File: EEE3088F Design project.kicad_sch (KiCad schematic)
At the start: 0 parts

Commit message: changes made
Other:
- added sheet motor connections (main.kicad_sch)
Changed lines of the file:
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@@
 		(comment 4 "Phila Haanyama, Hannah Owen")
+	)
+	(sheet
+		(at 53.34 41.91)
+		(size 34.29 24.13)
+		(exclude_from_sim no)
+		(in_bom yes)
+		(on_board yes)
+		(dnp no)
+		(fields_autoplaced yes)
+		(stroke
+			(width 0.1524)
+			(type solid)
+		)
+		(fill
+			(color 0 0 0 0.0000)
+		)
+		(property "Sheetname" "motor connections"
+			(at 53.34 41.1984 0)
+			(show_name yes)
+			(effects
+				(font
+					(size 1.27 1.27)
+				)
+				(justify left bottom)
+			)
+		)
+		(property "Sheetfile" "main.kicad_sch"
+			(at 53.34 66.6246 0)
+			(effects
+				(font
+					(size 1.27 1.27)
+				)
+				(justify left top)
+			)
+		)
+		(instances
+			(project "EEE3088F Design project"
+				(path "/d1463c6f-2f5e-4460-8cd2-c7ccf4d8def7"
+					(page "2")
+				)
+			)
+		)
 	)
 	(sheet_instances

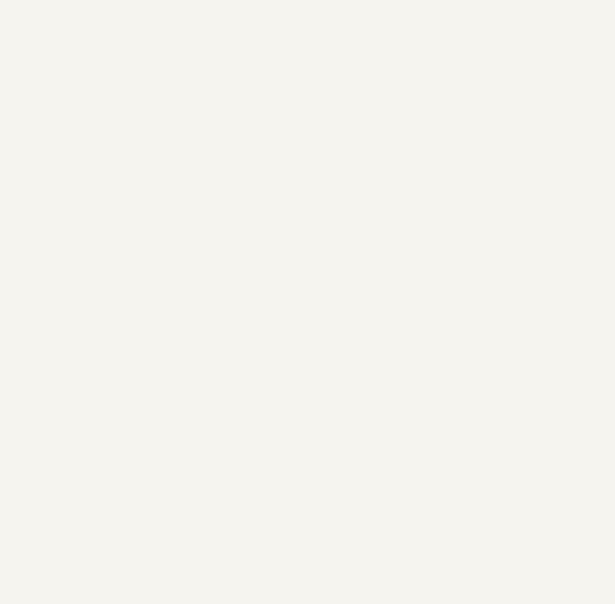
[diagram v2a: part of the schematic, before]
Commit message: Updated KiCad project files and removed old backups
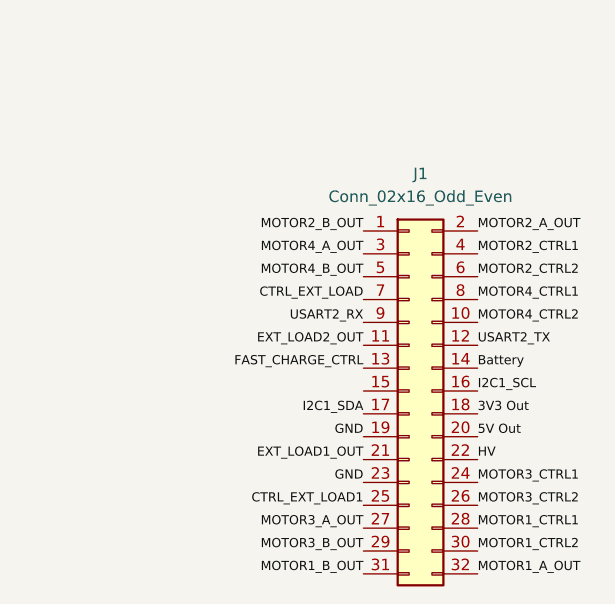
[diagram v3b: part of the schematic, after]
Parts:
- added J1: Conn_02x16_Odd_Even, symbol Connector_Generic:Conn_02x16_Odd_Even
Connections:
- new net 3V3 Out: J1.18 (Pin_18)
- new net 5V Out: J1.20 (Pin_20)
- new net Battery: J1.14 (Pin_14)
- new net CTRL_EXT_LOAD: J1.7 (Pin_7)
- new net CTRL_EXT_LOAD1: J1.25 (Pin_25)
- new net EXT_LOAD1_OUT: J1.21 (Pin_21)
- new net EXT_LOAD2_OUT: J1.11 (Pin_11)
- new net FAST_CHARGE_CTRL: J1.13 (Pin_13)
- new net GND: J1.19 (Pin_19), J1.23 (Pin_23)
- new net HV: J1.22 (Pin_22)
- new net I2C1_SCL: J1.16 (Pin_16)
- new net I2C1_SDA: J1.17 (Pin_17)
- new net MOTOR1_A_OUT: J1.32 (Pin_32)
- new net MOTOR1_B_OUT: J1.31 (Pin_31)
- new net MOTOR1_CTRL1: J1.28 (Pin_28)
- new net MOTOR1_CTRL2: J1.30 (Pin_30)
- new net MOTOR2_A_OUT: J1.2 (Pin_2)
- new net MOTOR2_B_OUT: J1.1 (Pin_1)
- new net MOTOR2_CTRL1: J1.4 (Pin_4)
- new net MOTOR2_CTRL2: J1.6 (Pin_6)
- new net MOTOR3_A_OUT: J1.27 (Pin_27)
- new net MOTOR3_B_OUT: J1.29 (Pin_29)
- new net MOTOR3_CTRL1: J1.24 (Pin_24)
- new net MOTOR3_CTRL2: J1.26 (Pin_26)
- new net MOTOR4_A_OUT: J1.3 (Pin_3)
- new net MOTOR4_B_OUT: J1.5 (Pin_5)
- new net MOTOR4_CTRL1: J1.8 (Pin_8)
- new net MOTOR4_CTRL2: J1.10 (Pin_10)
- new net USART2_RX: J1.9 (Pin_9)
- new net USART2_TX: J1.12 (Pin_12)

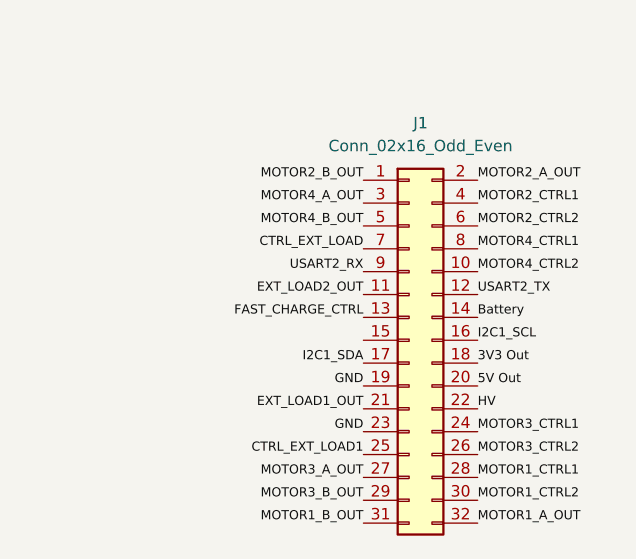
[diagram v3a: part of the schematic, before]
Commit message: DNP for 2x16 and global labels
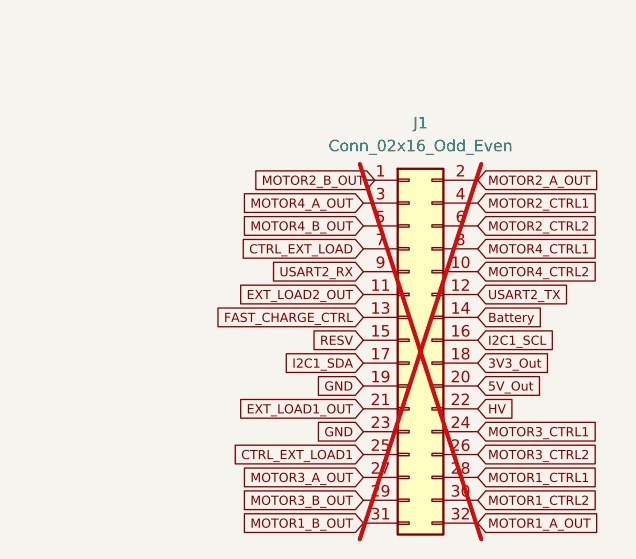
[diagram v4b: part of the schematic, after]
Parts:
- J1: now not fitted
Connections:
- net RESV: now reaches J1.15 (Pin_15)
- net 3V3 Out renamed 3V3_Out
- net 5V Out renamed 5V_Out

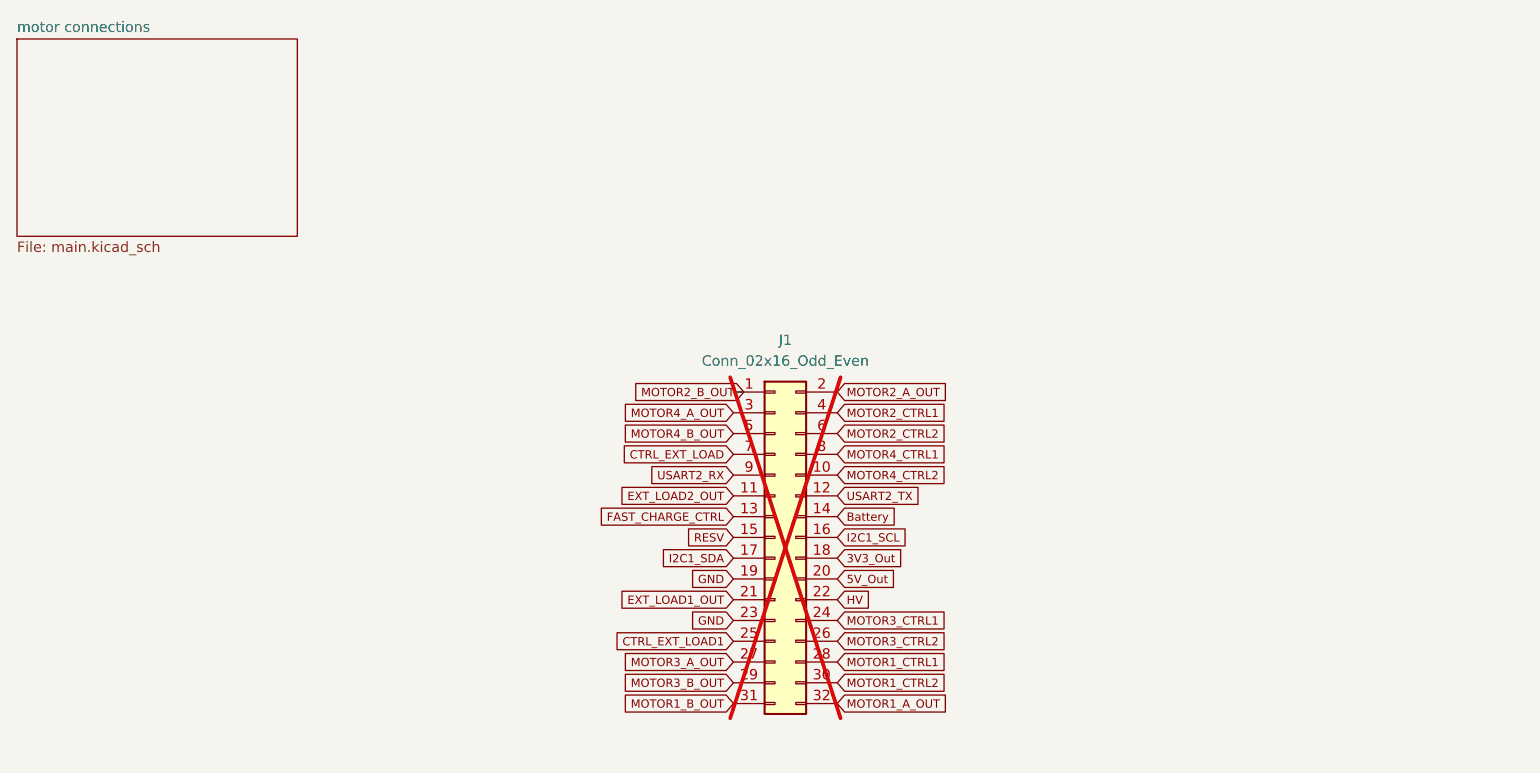
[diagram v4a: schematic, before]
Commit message: Removed old backups and updated KiCad files
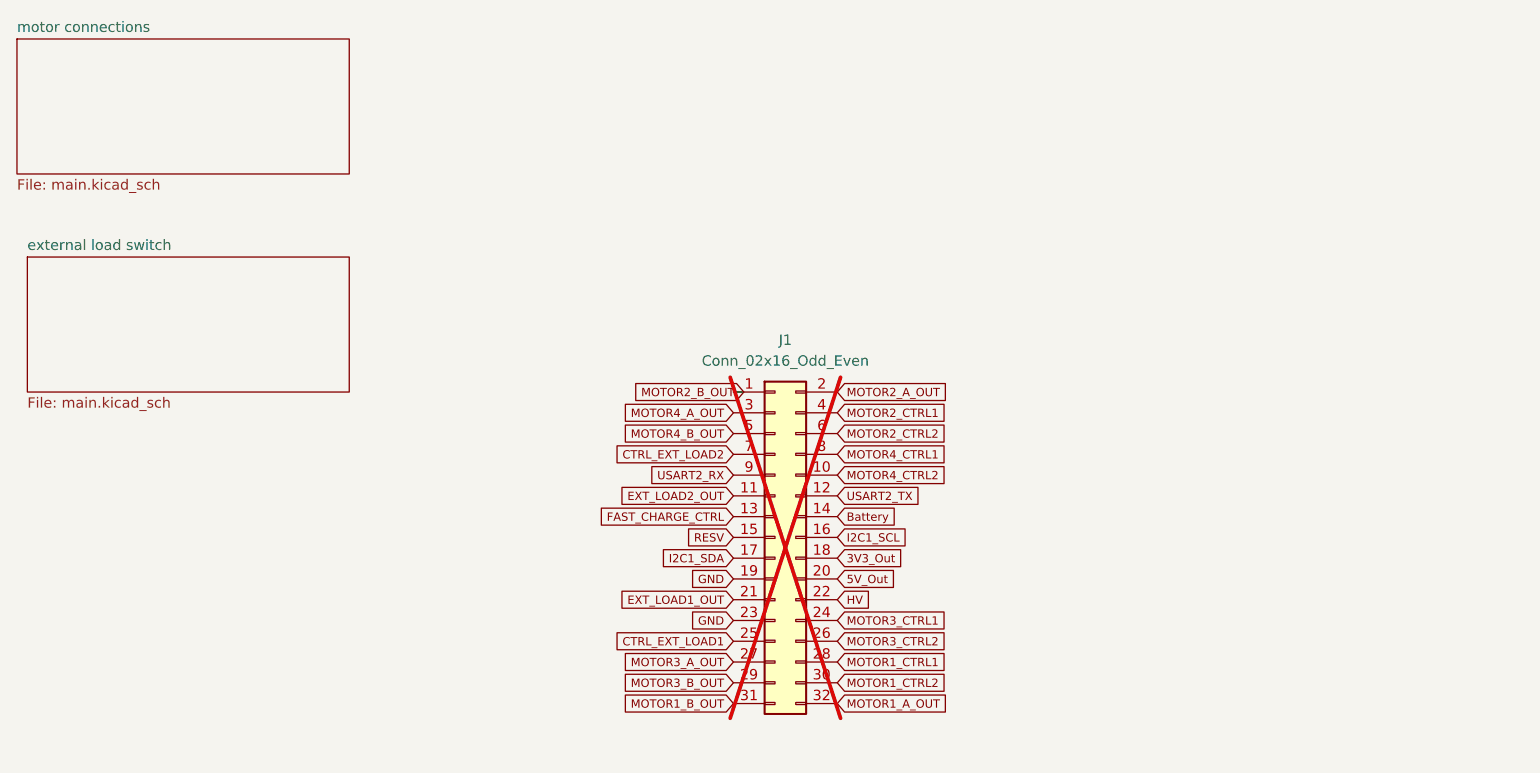
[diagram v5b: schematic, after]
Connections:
- net CTRL_EXT_LOAD renamed CTRL_EXT_LOAD2
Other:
- added sheet external load switch (main.kicad_sch)
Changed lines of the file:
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@@
 		)
 	)
-	(global_label "CTRL_EXT_LOAD"
+	(global_label "CTRL_EXT_LOAD2"
 		(shape input)
 		(at 140.97 92.71 180)
@@
 		)
 		(property "Intersheetrefs" "${INTERSHEET_REFS}"
-			(at 126.9706 92.71 0)
+			(at 126.003 92.71 0)
 			(effects
 				(font
@@
 	(sheet
 		(at 53.34 41.91)
-		(size 34.29 24.13)
+		(size 40.64 16.51)
 		(exclude_from_sim no)
 		(in_bom yes)
@@
 		)
 		(property "Sheetfile" "main.kicad_sch"
-			(at 53.34 66.6246 0)
+			(at 53.34 59.0046 0)
 			(effects
 				(font
@@
 				)
 			)
+		)
+	)
+	(sheet
+		(at 54.61 68.58)
+		(size 39.37 16.51)
+		(exclude_from_sim no)
+		(in_bom yes)
+		(on_board yes)
+		(dnp no)
+		(fields_autoplaced yes)
+		(stroke
+			(width 0.1524)
+			(type solid)
+		)
+		(fill
+			(color 0 0 0 0.0000)
+		)
+		(property "Sheetname" "external load switch"
+			(at 54.61 67.8684 0)
+			(show_name yes)
+			(effects
+				(font
+					(size 1.27 1.27)
+				)
+				(justify left bottom)
+			)
+		)
+		(property "Sheetfile" "main.kicad_sch"
+			(at 54.61 85.6746 0)
+			(effects
+				(font
+					(size 1.27 1.27)
+				)
+				(justify left top)
+			)
+		)
+		(instances
+			(project "EEE3088F Design project"
+				(path "/d1463c6f-2f5e-4460-8cd2-c7ccf4d8def7"
+					(page "3")
+				)
+			)

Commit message: added motor and INA219 circuits
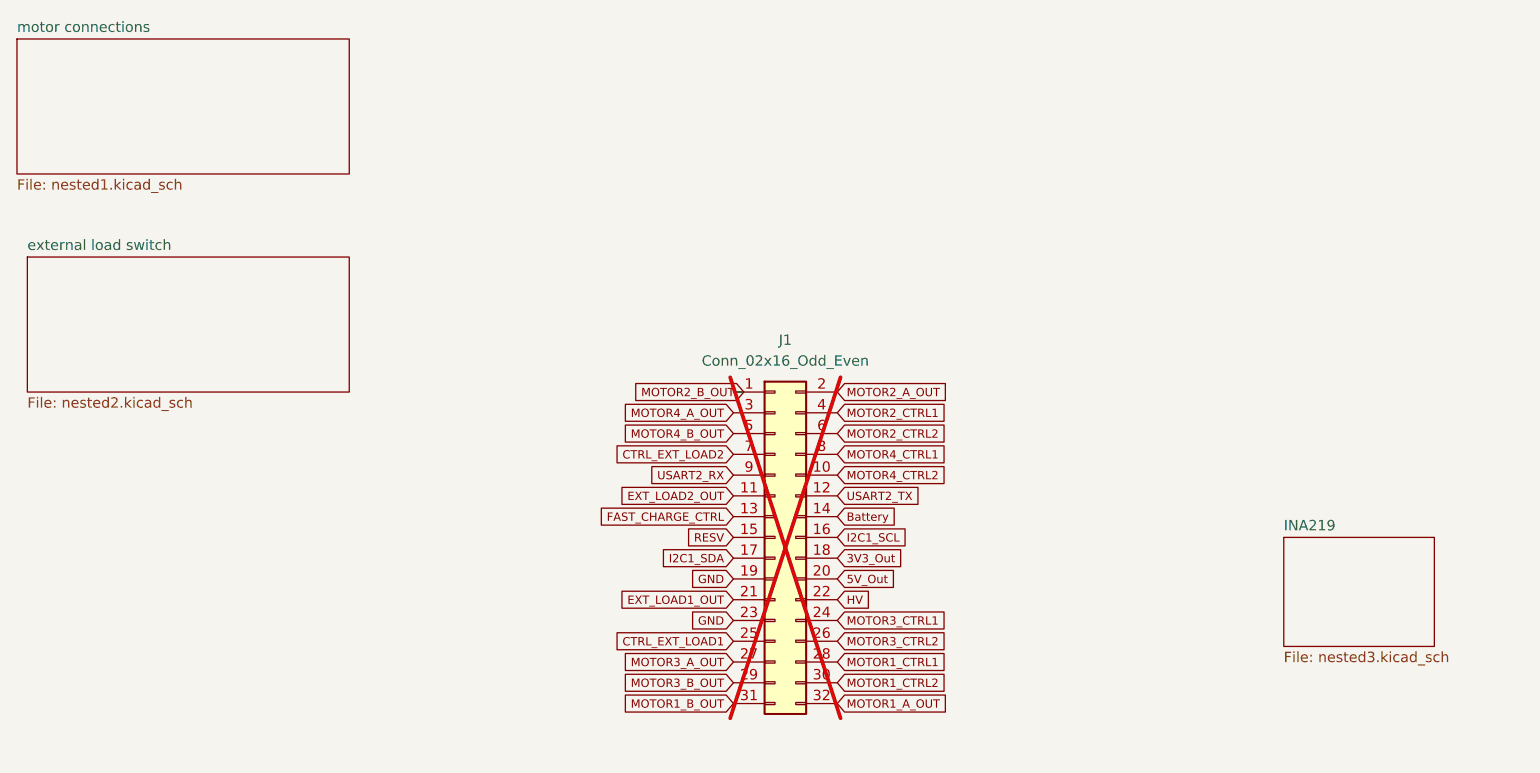
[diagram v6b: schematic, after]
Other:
- added sheet INA219 (nested3.kicad_sch)
- sheet external load switch: file main.kicad_sch -> nested2.kicad_sch
- sheet motor connections: file main.kicad_sch -> nested1.kicad_sch
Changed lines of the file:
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@@
 			)
 		)
-		(property "Sheetfile" "main.kicad_sch"
+		(property "Sheetfile" "nested1.kicad_sch"
 			(at 53.34 59.0046 0)
 			(effects
@@
 			)
 		)
-		(property "Sheetfile" "main.kicad_sch"
+		(property "Sheetfile" "nested2.kicad_sch"
 			(at 54.61 85.6746 0)
 			(effects
 				(font
+					(size 1.27 1.27)
+				)
+				(justify left top)
+			)
+		)
+		(instances
+			(project "EEE3088F Design project"
+				(path "/d1463c6f-2f5e-4460-8cd2-c7ccf4d8def7"
+					(page "3")
+				)
+			)
+		)
+	)
+	(sheet
+		(at 208.28 102.87)
+		(size 18.415 13.335)
+		(exclude_from_sim no)
+		(in_bom yes)
+		(on_board yes)
+		(dnp no)
+		(fields_autoplaced yes)
+		(stroke
+			(width 0.1524)
+			(type solid)
+		)
+		(fill
+			(color 0 0 0 0.0000)
+		)
+		(property "Sheetname" "INA219"
+			(at 208.28 102.1584 0)
+			(effects
+				(font
+					(size 1.27 1.27)
+				)
+				(justify left bottom)
+			)
+		)
+		(property "Sheetfile" "nested3.kicad_sch"
+			(at 208.28 116.7896 0)
+			(effects
+				(font

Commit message: made changes to USB circuit
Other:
- added sheet USB C (nested4.kicad_sch)
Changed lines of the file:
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@@
+		)
+	)
+	(sheet
+		(at 210.058 74.676)
+		(size 18.542 12.954)
+		(exclude_from_sim no)
+		(in_bom yes)
+		(on_board yes)
+		(dnp no)
+		(fields_autoplaced yes)
+		(stroke
+			(width 0.1524)
+			(type solid)
+		)
+		(fill
+			(color 0 0 0 0.0000)
+		)
+		(property "Sheetname" "USB C"
+			(at 210.058 73.9644 0)
+			(effects
+				(font
+					(size 1.27 1.27)
+				)
+				(justify left bottom)
+			)
+		)
+		(property "Sheetfile" "nested4.kicad_sch"
+			(at 210.058 88.2146 0)
+			(effects
+				(font
+					(size 1.27 1.27)
+				)
+				(justify left top)
+			)
+		)
+		(instances
+			(project "EEE3088F Design project"
+				(path "/d1463c6f-2f5e-4460-8cd2-c7ccf4d8def7"
+					(page "5")
+				)
+			)
 		)
 	)

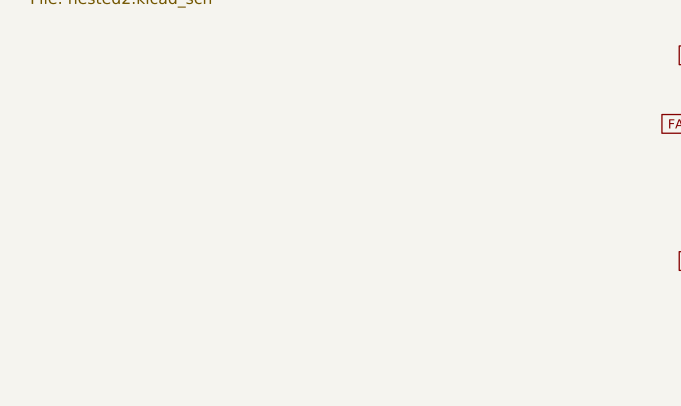
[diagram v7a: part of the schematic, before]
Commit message: Removed old backups and updated KiCad files
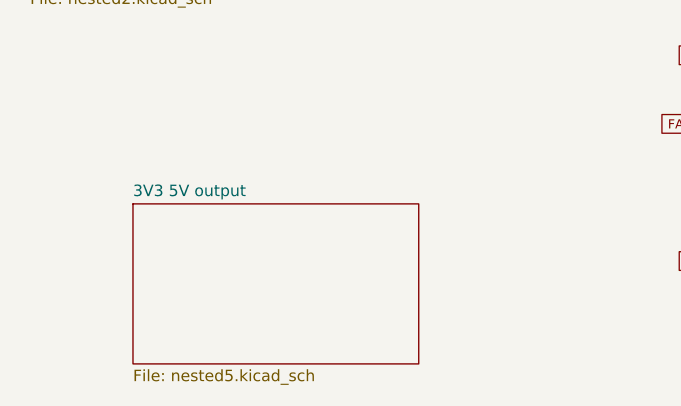
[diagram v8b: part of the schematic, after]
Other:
- added sheet 3V3 5V output (nested5.kicad_sch)
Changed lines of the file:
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@@
+	)
+	(sheet
+		(at 66.04 109.22)
+		(size 31.75 17.78)
+		(exclude_from_sim no)
+		(in_bom yes)
+		(on_board yes)
+		(dnp no)
+		(fields_autoplaced yes)
+		(stroke
+			(width 0.1524)
+			(type solid)
+		)
+		(fill
+			(color 0 0 0 0.0000)
+		)
+		(property "Sheetname" "3V3 5V output"
+			(at 66.04 108.5084 0)
+			(effects
+				(font
+					(size 1.27 1.27)
+				)
+				(justify left bottom)
+			)
+		)
+		(property "Sheetfile" "nested5.kicad_sch"
+			(at 66.04 127.5846 0)
+			(effects
+				(font
+					(size 1.27 1.27)
+				)
+				(justify left top)
+			)
+		)
+		(instances
+			(project "EEE3088F Design project"
+				(path "/d1463c6f-2f5e-4460-8cd2-c7ccf4d8def7"
+					(page "6")
+				)
+			)
+		)
 	)
 	(sheet
